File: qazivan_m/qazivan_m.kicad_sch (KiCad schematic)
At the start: 108 parts, among them J1 AVR-ISP-6, J3 Conn_01x04_Female, U1 ATmega32U4-AU, Y1 16MHz

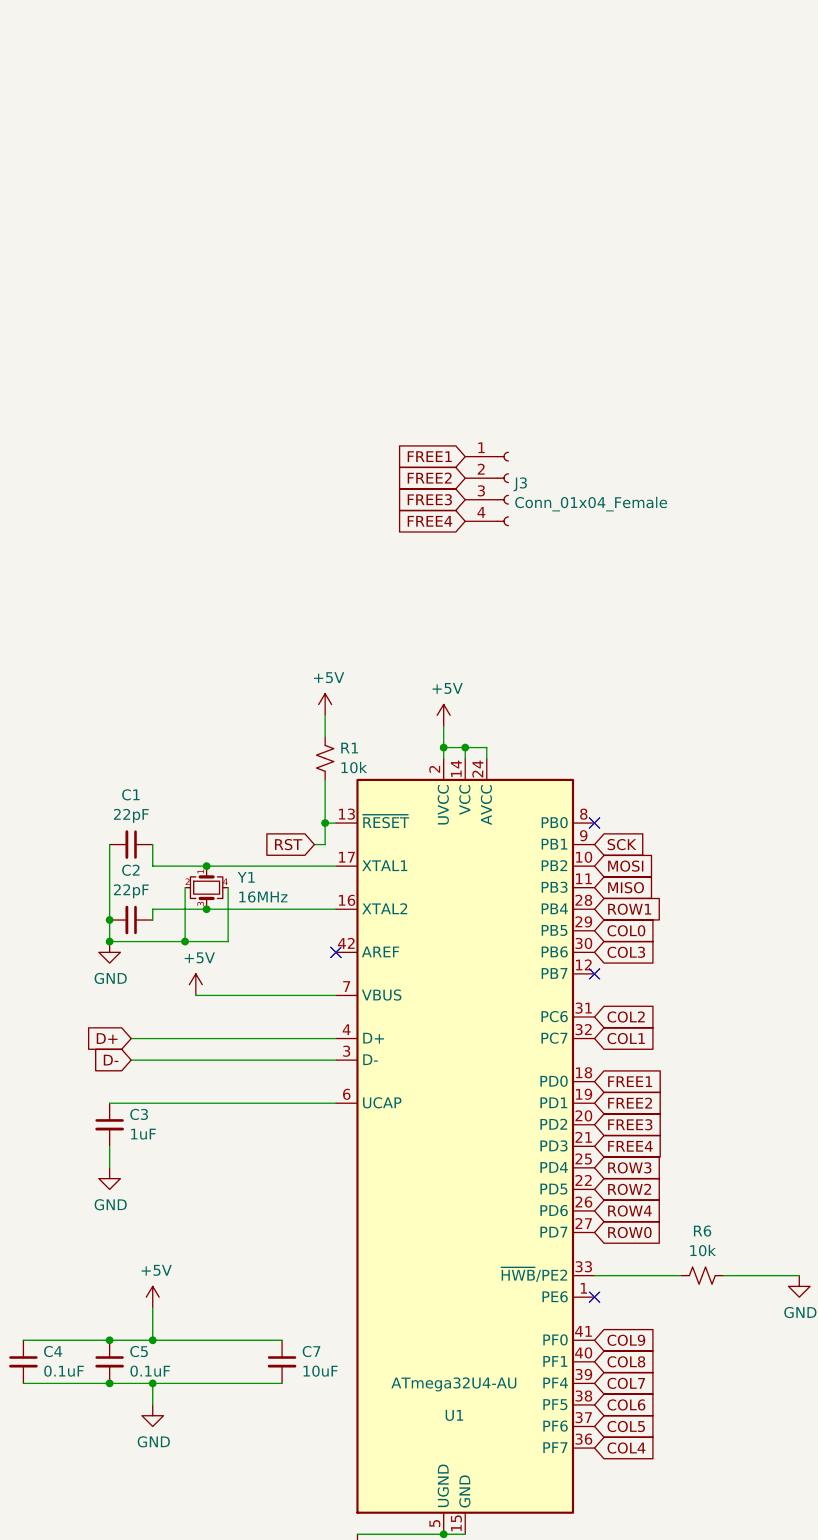
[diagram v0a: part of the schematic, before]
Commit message: add indicator leds. need to figure out mouting
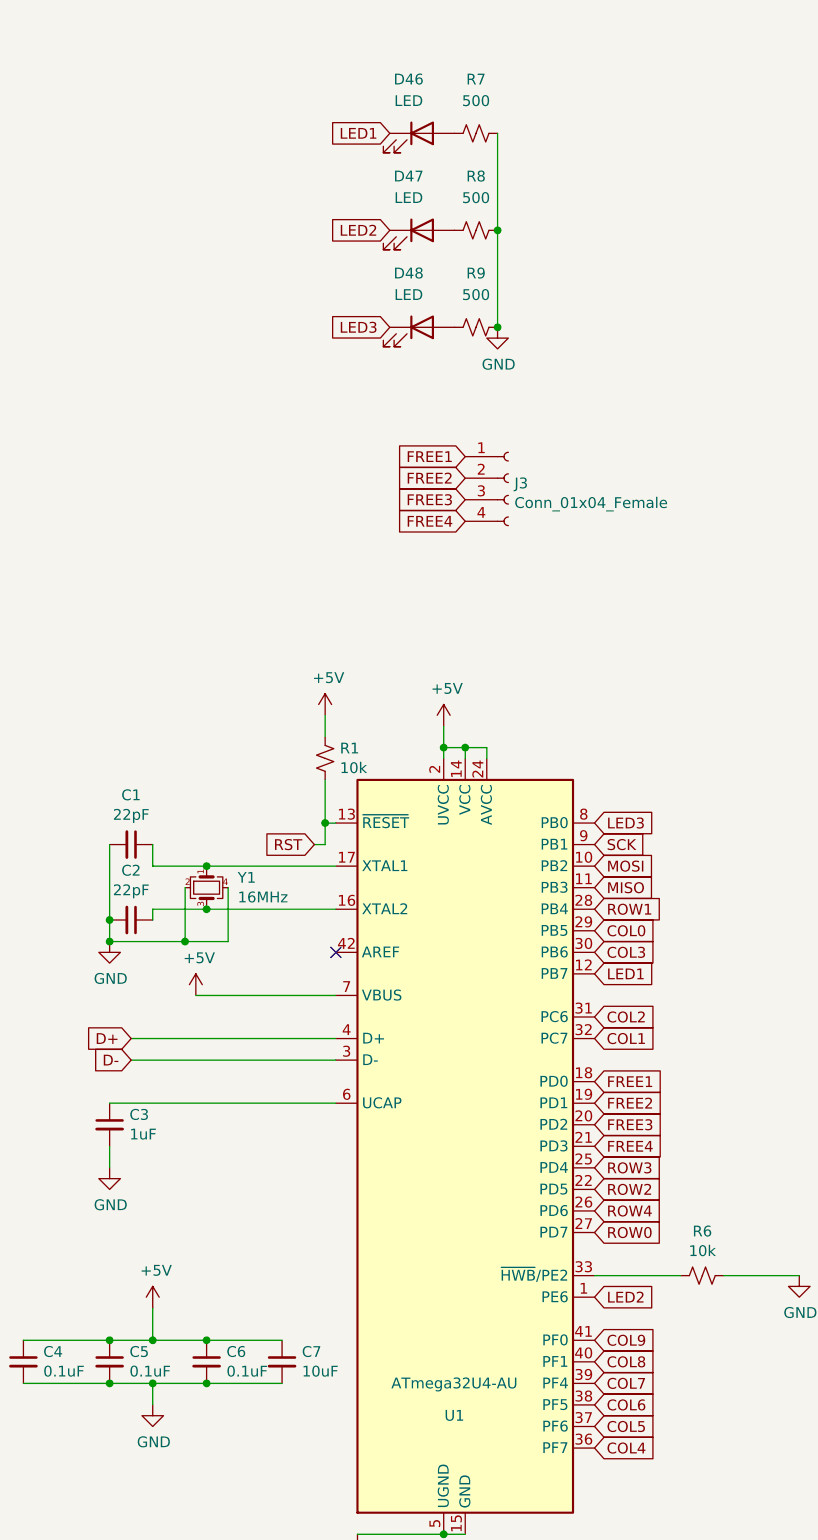
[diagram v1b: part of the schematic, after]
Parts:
- added C6: 0.1uF, Capacitor_SMD:C_0805_2012Metric, symbol Device:C_Small
- added D46, D47, D48: LED, LED_SMD:LED_0805_2012Metric, symbol Device:LED
- added R7, R8, R9: 500, Resistor_SMD:R_0805_2012Metric, symbol Device:R_Small_US
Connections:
- net +5V: now also C6.1
- net GND: now also C6.2, R7.2, R8.2, R9.2
- net LED2: now reaches U1.1 (PE6)
- net LED2: now also D47.1 (K)
- net LED1: now reaches U1.12 (PB7)
- net LED1: now also D46.1 (K)
- net LED3: now reaches U1.8 (PB0)
- net LED3: now also D48.1 (K)
- new net: D47.2 (A), R8.1
- new net: D48.2 (A), R9.1
- new net: D46.2 (A), R7.1
- no-connect marks 6 -> 3

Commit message: fix indicator leds
mcu pin to anode not cathode
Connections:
- net LED1: now also D46.2 (A); no longer D46.1 (K)
- net LED2: now also D47.2 (A); no longer D47.1 (K)
- net LED3: now also D48.2 (A); no longer D48.1 (K)
- net at R8.1: now also D47.1 (K); no longer D47.2 (A)
- net at R9.1: now also D48.1 (K); no longer D48.2 (A)
- net at R7.1: now also D46.1 (K); no longer D46.2 (A)
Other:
- moved on the sheet: D46, D47, D48
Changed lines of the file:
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@@
     (pin "4")
   )
-  (symbol (lib_id "Device:LED") (at 60.96 38.1 0) (unit 1)
-    (in_bom yes) (on_board yes) (fields_autoplaced)
-    (property "Reference" "D47" (id 0) (at 59.3725 31.75 0))
-    (property "Value" "LED" (id 1) (at 59.3725 34.29 0))
+  (symbol (lib_id "Device:LED") (at 60.96 38.1 180) (unit 1)
+    (in_bom yes) (on_board yes) (fields_autoplaced)
+    (property "Reference" "D47" (id 0) (at 62.5475 30.48 0))
+    (property "Value" "LED" (id 1) (at 62.5475 33.02 0))
     (property "Footprint" "LED_SMD:LED_0805_2012Metric" (id 2) (at 60.96 38.1 0)
       (effects (font (size 1.27 1.27)) hide)
@@
     (pin "2")
   )
-  (symbol (lib_id "Device:LED") (at 60.96 26.67 0) (unit 1)
-    (in_bom yes) (on_board yes) (fields_autoplaced)
-    (property "Reference" "D46" (id 0) (at 59.3725 20.32 0))
-    (property "Value" "LED" (id 1) (at 59.3725 22.86 0))
+  (symbol (lib_id "Device:LED") (at 60.96 26.67 180) (unit 1)
+    (in_bom yes) (on_board yes) (fields_autoplaced)
+    (property "Reference" "D46" (id 0) (at 62.5475 19.05 0))
+    (property "Value" "LED" (id 1) (at 62.5475 21.59 0))
     (property "Footprint" "LED_SMD:LED_0805_2012Metric" (id 2) (at 60.96 26.67 0)
       (effects (font (size 1.27 1.27)) hide)
@@
     (pin "2")
   )
-  (symbol (lib_id "Device:LED") (at 60.96 49.53 0) (unit 1)
-    (in_bom yes) (on_board yes) (fields_autoplaced)
-    (property "Reference" "D48" (id 0) (at 59.3725 43.18 0))
-    (property "Value" "LED" (id 1) (at 59.3725 45.72 0))
+  (symbol (lib_id "Device:LED") (at 60.96 49.53 180) (unit 1)
+    (in_bom yes) (on_board yes) (fields_autoplaced)
+    (property "Reference" "D48" (id 0) (at 62.5475 41.91 0))
+    (property "Value" "LED" (id 1) (at 62.5475 44.45 0))
     (property "Footprint" "LED_SMD:LED_0805_2012Metric" (id 2) (at 60.96 49.53 0)
       (effects (font (size 1.27 1.27)) hide)

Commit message: update bottom row
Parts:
- MX33: footprint MX_Only:MXOnly-1U-Hotswap -> MX_Only:MXOnly-2.25U-Hotswap-ReversedStabilizers
- MX34: footprint MX_Only:MXOnly-2.25U-Hotswap-ReversedStabilizers -> MX_Only:MXOnly-2U-Hotswap-ReversedStabilizers
- MX35: footprint MX_Only:MXOnly-2U-Hotswap-ReversedStabilizers -> MX_Only:MXOnly-1U-Hotswap
- MX38: footprint MX_Only:MXOnly-6.25U-Hotswap-ReversedStabilizers -> MX_Only:MXOnly-6.25U-Hotswap
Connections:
- net COL4: no longer MX34.1 (COL)
- net COL5: now also MX34.1 (COL); no longer MX35.1 (COL)
- net COL7: now also MX35.1 (COL); no longer MX36.1 (COL)
- net COL8: now also MX36.1 (COL)
- net at D34.2 (A), MX34.2 (ROW): now also MX38.2 (ROW)
- net at D35.2 (A), MX35.2 (ROW): no longer MX38.2 (ROW)
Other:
- moved on the sheet: D34, D35, D36, MX34, MX35, MX36

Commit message: center big bar
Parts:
- MX45: renamed from MX38; footprint MX_Only:MXOnly-6.25U-Hotswap -> MX_Only:MXOnly-6.25U-Hotswap-ReversedStabilizers
- renumbered D46 to D1, D1 to D10, D2 to D11, D3 to D12, D4 to D13, D5 to D14, D6 to D15, D7 to D16, D8 to D17, D9 to D18, D10 to D19, D40 to D2, D11 to D20, D12 to D21, D13 to D22, D14 to D23, D15 to D24, D16 to D25, D17 to D26, D18 to D27, D19 to D28, D20 to D29, D41 to D3, D21 to D30, D22 to D31, D23 to D32, D24 to D33, D25 to D34, D26 to D35, D27 to D36, D28 to D37, D39 to D38, D29 to D39, D42 to D4, D30 to D40, D31 to D41, D32 to D42, D33 to D43, D34 to D44, D35 to D45, D36 to D46, D37 to D47, D38 to D48, D43 to D5, D44 to D6, D45 to D7, D47 to D8, D48 to D9, J3 to J1, J1 to J2, MX40 to MX1, MX4 to MX10, MX5 to MX11, MX6 to MX12, MX7 to MX13, MX8 to MX14, MX9 to MX15, MX10 to MX16, MX11 to MX17, MX12 to MX18, MX13 to MX19, MX41 to MX2, MX14 to MX20, MX15 to MX21, MX16 to MX22, MX17 to MX23, MX18 to MX24, MX19 to MX25, MX20 to MX26, MX21 to MX27, MX22 to MX28, MX23 to MX29, MX42 to MX3, MX24 to MX30, MX25 to MX31, MX26 to MX32, MX27 to MX33, MX28 to MX34, MX39 to MX35, MX29 to MX36, MX30 to MX37, MX31 to MX38, MX32 to MX39, MX43 to MX4, MX33 to MX40, MX34 to MX41, MX35 to MX42, MX36 to MX43, MX37 to MX44, MX44 to MX5, MX45 to MX6, MX1 to MX7, MX2 to MX8, MX3 to MX9, R7 to R1, R8 to R2, R9 to R3, R1 to R4, R2 to R5, R3 to R6, R4 to R7, R5 to R8, R6 to R9
